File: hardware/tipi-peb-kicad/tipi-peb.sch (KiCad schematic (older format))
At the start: 48 parts, among them Q1 Q_NPN_BCE, T1 TEST_1P, T2 TEST_1P, T3 TEST_1P, T4 TEST_1P, T5 TEST_1P, U1 74HCT138, U2 27C256, U3 74HCT244, U4 74HCT244, U5 74HCT244, U6 XC95144XL-TQ100, U7 74HCT245, U8 LM1117-3.3, U9 LM7805_TO220

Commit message: spread footprints out on peb pcboard.
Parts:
- JTAG1, RPi1: footprint Connect:IDC_Header_Straight_10pins -> Pin_Headers:Pin_Header_Straight_2x05_Pitch2.54mm
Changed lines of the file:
@@
 F 0 "JTAG1" H 14480 1830 50  0000 C CNN
 F 1 "AVR-JTAG-10" H 14310 1170 50  0000 L BNN
-F 2 "Connect:IDC_Header_Straight_10pins" V 14080 1520 50  0001 C CNN
+F 2 "Pin_Headers:Pin_Header_Straight_2x05_Pitch2.54mm" V 14080 1520 50  0001 C CNN
 F 3 "" H 14650 1500 50  0001 C CNN
 	1    14650 1500
@@
 F 0 "RPi1" H 14350 3300 50  0000 C CNN
 F 1 "RPI_CONN_02X05" H 14350 2700 50  0000 C CNN
-F 2 "Connect:IDC_Header_Straight_10pins" H 14350 1800 50  0001 C CNN
+F 2 "Pin_Headers:Pin_Header_Straight_2x05_Pitch2.54mm" H 14350 1800 50  0001 C CNN
 F 3 "" H 14350 1800 50  0001 C CNN
 	1    14350 3000

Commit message: a little layout progress
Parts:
- U1: footprint SMD_Packages:SO-16-W -> Housings_SSOP:SSOP-16_5.3x6.2mm_Pitch0.65mm
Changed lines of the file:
@@
 F 0 "U1" H 1950 9800 50  0000 C CNN
 F 1 "74HCT138" H 2000 8751 50  0000 C CNN
-F 2 "SMD_Packages:SO-16-W" H 1850 9300 50  0001 C CNN
+F 2 "Housings_SSOP:SSOP-16_5.3x6.2mm_Pitch0.65mm" H 1850 9300 50  0001 C CNN
 F 3 "" H 1850 9300 50  0001 C CNN
 	1    1850 9300

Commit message: stash these changes.
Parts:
- U1: footprint Housings_SSOP:SSOP-16_5.3x6.2mm_Pitch0.65mm -> Housings_SSOP:SSOP-16_4.4x5.2mm_Pitch0.65mm
- U3, U4, U5, U7: footprint SMD_Packages:SSOP-20 -> Housings_SSOP:SSOP-20_4.4x6.5mm_Pitch0.65mm
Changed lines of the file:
@@
 F 0 "U7" H 10350 9975 50  0000 L BNN
 F 1 "74HCT245" H 10300 8825 50  0000 L TNN
-F 2 "SMD_Packages:SSOP-20" H 10250 9400 50  0001 C CNN
+F 2 "Housings_SSOP:SSOP-20_4.4x6.5mm_Pitch0.65mm" H 10250 9400 50  0001 C CNN
 F 3 "" H 10250 9400 50  0001 C CNN
 	1    10250 9400
@@
 F 0 "U5" H 8250 10050 50  0000 L CNN
 F 1 "74HCT244" H 8200 8750 50  0000 L CNN
-F 2 "SMD_Packages:SSOP-20" H 8150 9400 50  0001 C CNN
+F 2 "Housings_SSOP:SSOP-20_4.4x6.5mm_Pitch0.65mm" H 8150 9400 50  0001 C CNN
 F 3 "" H 8150 9400 50  0000 C CNN
 	1    8150 9400
@@
 F 0 "U4" H 5900 10050 50  0000 L CNN
 F 1 "74HCT244" H 5850 8750 50  0000 L CNN
-F 2 "SMD_Packages:SSOP-20" H 5800 9400 50  0001 C CNN
+F 2 "Housings_SSOP:SSOP-20_4.4x6.5mm_Pitch0.65mm" H 5800 9400 50  0001 C CNN
 F 3 "" H 5800 9400 50  0000 C CNN
 	1    5800 9400
@@
 F 0 "U3" H 3850 10050 50  0000 L CNN
 F 1 "74HCT244" H 3800 8750 50  0000 L CNN
-F 2 "SMD_Packages:SSOP-20" H 3750 9400 50  0001 C CNN
+F 2 "Housings_SSOP:SSOP-20_4.4x6.5mm_Pitch0.65mm" H 3750 9400 50  0001 C CNN
 F 3 "" H 3750 9400 50  0000 C CNN
 	1    3750 9400
@@
 F 0 "U1" H 1950 9800 50  0000 C CNN
 F 1 "74HCT138" H 2000 8751 50  0000 C CNN
-F 2 "Housings_SSOP:SSOP-16_5.3x6.2mm_Pitch0.65mm" H 1850 9300 50  0001 C CNN
+F 2 "Housings_SSOP:SSOP-16_4.4x5.2mm_Pitch0.65mm" H 1850 9300 50  0001 C CNN
 F 3 "" H 1850 9300 50  0001 C CNN
 	1    1850 9300

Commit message: about half routed
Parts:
- removed T1, T2, T3, T4, T5: TEST_1P, Wire_Pads:SolderWirePad_single_0-8mmDrill, symbol TEST_1P
- U1: footprint Housings_SSOP:SSOP-16_4.4x5.2mm_Pitch0.65mm -> Housings_SSOP:TSSOP-16_4.4x5mm_Pitch0.65mm
- U3, U4, U5, U7: footprint Housings_SSOP:SSOP-20_4.4x6.5mm_Pitch0.65mm -> Housings_SSOP:TSSOP-20_4.4x6.5mm_Pitch0.65mm
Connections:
- no-connect marks 61 -> 66
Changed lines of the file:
@@
 F 0 "U7" H 10350 9975 50  0000 L BNN
 F 1 "74HCT245" H 10300 8825 50  0000 L TNN
-F 2 "Housings_SSOP:SSOP-20_4.4x6.5mm_Pitch0.65mm" H 10250 9400 50  0001 C CNN
+F 2 "Housings_SSOP:TSSOP-20_4.4x6.5mm_Pitch0.65mm" H 10250 9400 50  0001 C CNN
 F 3 "" H 10250 9400 50  0001 C CNN
 	1    10250 9400
@@
 $EndComp
 $Comp
-L TEST_1P T5
-U 1 1 597515DC
-P 14650 2800
-F 0 "T5" H 14650 3070 50  0000 C CNN
-F 1 "TEST_1P" H 14650 3000 50  0000 C CNN
-F 2 "Wire_Pads:SolderWirePad_single_0-8mmDrill" H 14850 2800 50  0001 C CNN
-F 3 "" H 14850 2800 50  0001 C CNN
-	1    14650 2800
-	1    0    0    -1
-$EndComp
-$Comp
-L TEST_1P T4
-U 1 1 5975362C
-P 10200 5600
-F 0 "T4" H 10200 5870 50  0000 C CNN
-F 1 "TEST_1P" H 10200 5800 50  0000 C CNN
-F 2 "Wire_Pads:SolderWirePad_single_0-8mmDrill" H 10400 5600 50  0001 C CNN
-F 3 "" H 10400 5600 50  0001 C CNN
-	1    10200 5600
-	0    1    1    0
-$EndComp
-$Comp
-L TEST_1P T3
-U 1 1 5975393E
-P 10200 5500
-F 0 "T3" H 10200 5770 50  0000 C CNN
-F 1 "TEST_1P" H 10200 5700 50  0000 C CNN
-F 2 "Wire_Pads:SolderWirePad_single_0-8mmDrill" H 10400 5500 50  0001 C CNN
-F 3 "" H 10400 5500 50  0001 C CNN
-	1    10200 5500
-	0    1    1    0
-$EndComp
-$Comp
-L TEST_1P T2
-U 1 1 597539A7
-P 10200 5400
-F 0 "T2" H 10200 5670 50  0000 C CNN
-F 1 "TEST_1P" H 10200 5600 50  0000 C CNN
-F 2 "Wire_Pads:SolderWirePad_single_0-8mmDrill" H 10400 5400 50  0001 C CNN
-F 3 "" H 10400 5400 50  0001 C CNN
-	1    10200 5400
-	0    1    1    0
-$EndComp
-$Comp
-L TEST_1P T1
-U 1 1 59753A11
-P 10200 5300
-F 0 "T1" H 10200 5570 50  0000 C CNN
-F 1 "TEST_1P" H 10200 5500 50  0000 C CNN
-F 2 "Wire_Pads:SolderWirePad_single_0-8mmDrill" H 10400 5300 50  0001 C CNN
-F 3 "" H 10400 5300 50  0001 C CNN
-	1    10200 5300
-	0    1    1    0
-$EndComp
-$Comp
 L R R4
 U 1 1 599E6C64
@@
 F 0 "U5" H 8250 10050 50  0000 L CNN
 F 1 "74HCT244" H 8200 8750 50  0000 L CNN
-F 2 "Housings_SSOP:SSOP-20_4.4x6.5mm_Pitch0.65mm" H 8150 9400 50  0001 C CNN
+F 2 "Housings_SSOP:TSSOP-20_4.4x6.5mm_Pitch0.65mm" H 8150 9400 50  0001 C CNN
 F 3 "" H 8150 9400 50  0000 C CNN
 	1    8150 9400
@@
 F 0 "U4" H 5900 10050 50  0000 L CNN
 F 1 "74HCT244" H 5850 8750 50  0000 L CNN
-F 2 "Housings_SSOP:SSOP-20_4.4x6.5mm_Pitch0.65mm" H 5800 9400 50  0001 C CNN
+F 2 "Housings_SSOP:TSSOP-20_4.4x6.5mm_Pitch0.65mm" H 5800 9400 50  0001 C CNN
 F 3 "" H 5800 9400 50  0000 C CNN
 	1    5800 9400
@@
 F 0 "U3" H 3850 10050 50  0000 L CNN
 F 1 "74HCT244" H 3800 8750 50  0000 L CNN
-F 2 "Housings_SSOP:SSOP-20_4.4x6.5mm_Pitch0.65mm" H 3750 9400 50  0001 C CNN
+F 2 "Housings_SSOP:TSSOP-20_4.4x6.5mm_Pitch0.65mm" H 3750 9400 50  0001 C CNN
 F 3 "" H 3750 9400 50  0000 C CNN
 	1    3750 9400
@@
 Connection ~ 8850 7000
 Wire Wire Line
-	9750 5600 10200 5600
-Wire Wire Line
-	9750 5500 10200 5500
-Wire Wire Line
-	9750 5400 10200 5400
-Wire Wire Line
-	9750 5300 10200 5300
-Wire Wire Line
 	11600 2150 11450 2150
 Wire Wire Line
@@
 F 0 "U1" H 1950 9800 50  0000 C CNN
 F 1 "74HCT138" H 2000 8751 50  0000 C CNN
-F 2 "Housings_SSOP:SSOP-16_4.4x5.2mm_Pitch0.65mm" H 1850 9300 50  0001 C CNN
+F 2 "Housings_SSOP:TSSOP-16_4.4x5mm_Pitch0.65mm" H 1850 9300 50  0001 C CNN
 F 3 "" H 1850 9300 50  0001 C CNN
 	1    1850 9300
@@
 	-1   0    0    1
 $EndComp
+NoConn ~ 9750 5300
+NoConn ~ 9750 5400
+NoConn ~ 9750 5500
+NoConn ~ 9750 5600
+NoConn ~ 14650 2800
 $EndSCHEMATC

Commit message: 2/3rds routed
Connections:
- net +5V: no longer R10.2
- net GND: no longer R11.2
- net TI_AMD: no longer E1.56 (MEMEN*), U1.4 (E1)
- new net TI_MEMEN: E1.56 (MEMEN*), U1.4 (E1)
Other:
- moved on the sheet: R10, R11
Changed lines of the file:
@@
 Text GLabel 2300 6700 2    60   Output ~ 0
 TI_PH3
-Text GLabel 1250 9650 0    60   Input ~ 0
+Text GLabel 1000 9650 0    60   Input ~ 0
 TI_MEMEN
 Text GLabel 4250 8900 2    60   Output ~ 0
@@
 Text GLabel 1200 4700 0    60   Output ~ 0
 TI_AME
-Text GLabel 1050 9550 0    60   Input ~ 0
+Text GLabel 900  9550 0    60   Input ~ 0
 TI_AMD
-Text GLabel 1050 9450 0    60   Input ~ 0
+Text GLabel 900  9450 0    60   Input ~ 0
 TI_AME
 Wire Wire Line
@@
 L R R10
 U 1 1 59EF200E
-P 1100 9950
-F 0 "R10" V 1180 9950 50  0000 C CNN
-F 1 "4.7k" V 1100 9950 50  0000 C CNN
-F 2 "Resistors_SMD:R_0805_HandSoldering" V 1030 9950 50  0001 C CNN
-F 3 "" H 1100 9950 50  0001 C CNN
-	1    1100 9950
+P 1050 9950
+F 0 "R10" V 1130 9950 50  0000 C CNN
+F 1 "4.7k" V 1050 9950 50  0000 C CNN
+F 2 "Resistors_SMD:R_0805_HandSoldering" V 980 9950 50  0001 C CNN
+F 3 "" H 1050 9950 50  0001 C CNN
+	1    1050 9950
 	1    0    0    -1
 $EndComp
@@
 L R R11
 U 1 1 59EF20E5
-P 1250 9950
-F 0 "R11" V 1330 9950 50  0000 C CNN
-F 1 "4.7k" V 1250 9950 50  0000 C CNN
-F 2 "Resistors_SMD:R_0805_HandSoldering" V 1180 9950 50  0001 C CNN
-F 3 "" H 1250 9950 50  0001 C CNN
-	1    1250 9950
+P 1200 9950
+F 0 "R11" V 1280 9950 50  0000 C CNN
+F 1 "4.7k" V 1200 9950 50  0000 C CNN
+F 2 "Resistors_SMD:R_0805_HandSoldering" V 1130 9950 50  0001 C CNN
+F 3 "" H 1200 9950 50  0001 C CNN
+	1    1200 9950
 	1    0    0    -1
 $EndComp
@@
 L GND #PWR050
 U 1 1 59EF22F3
-P 1250 10100
-F 0 "#PWR050" H 1250 9850 50  0001 C CNN
-F 1 "GND" H 1250 9950 50  0000 C CNN
-F 2 "" H 1250 10100 50  0001 C CNN
-F 3 "" H 1250 10100 50  0001 C CNN
-	1    1250 10100
+P 1200 10150
+F 0 "#PWR050" H 1200 9900 50  0001 C CNN
+F 1 "GND" H 1200 10000 50  0000 C CNN
+F 2 "" H 1200 10150 50  0001 C CNN
+F 3 "" H 1200 10150 50  0001 C CNN
+	1    1200 10150
 	1    0    0    -1
 $EndComp
@@
 L +5V #PWR051
 U 1 1 59EF241E
-P 1100 10100
-F 0 "#PWR051" H 1100 9950 50  0001 C CNN
-F 1 "+5V" H 1100 10240 50  0000 C CNN
-F 2 "" H 1100 10100 50  0001 C CNN
-F 3 "" H 1100 10100 50  0001 C CNN
-	1    1100 10100
+P 1050 10150
+F 0 "#PWR051" H 1050 10000 50  0001 C CNN
+F 1 "+5V" H 1050 10290 50  0000 C CNN
+F 2 "" H 1050 10150 50  0001 C CNN
+F 3 "" H 1050 10150 50  0001 C CNN
+	1    1050 10150
 	-1   0    0    1
 $EndComp
-Wire Wire Line
-	1250 9800 1250 9550
-Wire Wire Line
-	1250 9550 1050 9550
-Wire Wire Line
-	1100 9800 1100 9450
-Wire Wire Line
-	1050 9450 1250 9450
-Connection ~ 1100 9450
-Connection ~ 1250 9550
 $Comp
 L GND #PWR052
@@
 NoConn ~ 9750 5600
 NoConn ~ 14650 2800
+Wire Wire Line
+	1000 9650 1250 9650
+Wire Wire Line
+	1200 9800 1200 9550
+Wire Wire Line
+	900  9550 1250 9550
+Connection ~ 1200 9550
+Wire Wire Line
+	1250 9450 900  9450
+Wire Wire Line
+	1050 9800 1050 9450
+Connection ~ 1050 9450
 $EndSCHEMATC

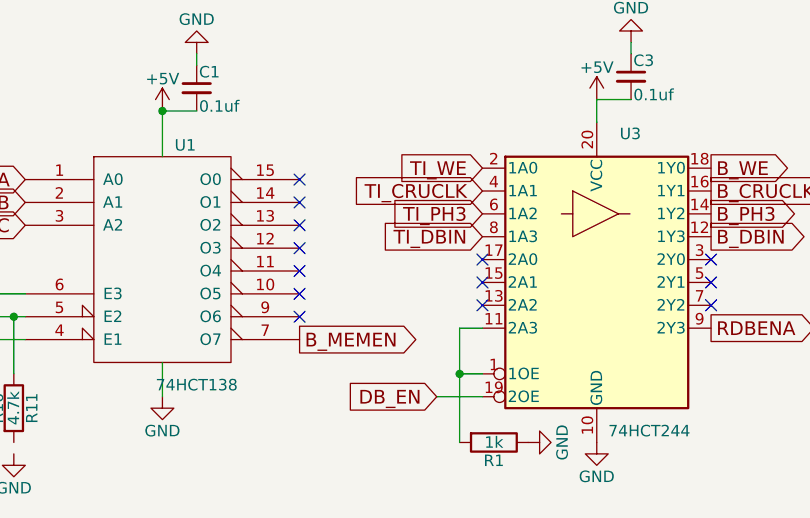
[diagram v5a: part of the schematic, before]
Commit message: just power lines left
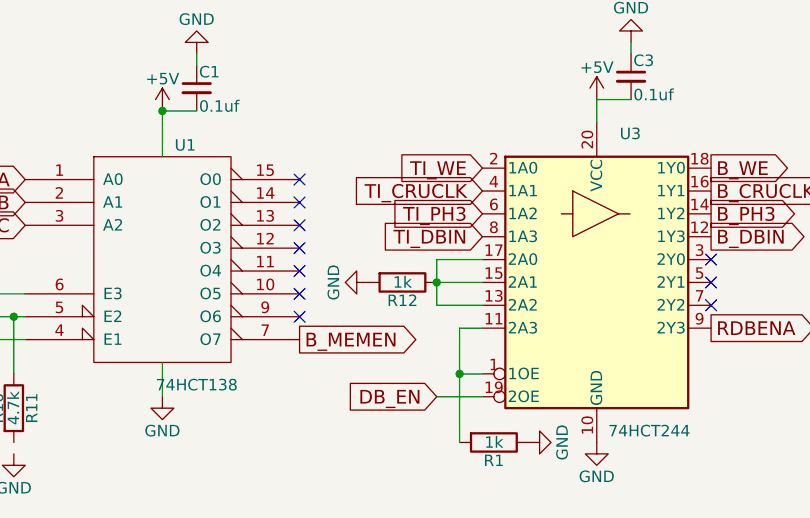
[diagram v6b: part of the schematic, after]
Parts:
- added R12: 1k, Resistors_SMD:R_0805_HandSoldering, symbol R
- U8, U9: footprint TO_SOT_Packages_SMD:SOT-223 -> TO_SOT_Packages_SMD:SOT-223-3_TabPin2
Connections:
- net GND: now also R12.2
- net at U3.13 (2A2): now also U3.15 (2A1), U3.17 (2A0), R12.1
- no-connect marks 66 -> 63
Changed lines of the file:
@@
 F 0 "U8" H 14550 4000 50  0000 C CNN
 F 1 "LM1117-3.3" H 14450 4500 50  0000 C CNN
-F 2 "TO_SOT_Packages_SMD:SOT-223" H 14450 4250 50  0001 C CNN
+F 2 "TO_SOT_Packages_SMD:SOT-223-3_TabPin2" H 14450 4250 50  0001 C CNN
 F 3 "" H 14450 4250 50  0001 C CNN
 	1    14450 4250
@@
 F 0 "U9" H 14300 5325 50  0000 C CNN
 F 1 "LM7805_TO220" H 14450 5325 50  0000 L CNN
-F 2 "TO_SOT_Packages_SMD:SOT-223" H 14450 5425 50  0001 C CIN
+F 2 "TO_SOT_Packages_SMD:SOT-223-3_TabPin2" H 14450 5425 50  0001 C CIN
 F 3 "" H 14450 5150 50  0001 C CNN
 	1    14450 5200
@@
 	0    1    1    0
 $EndComp
-NoConn ~ 3250 9300
-NoConn ~ 3250 9400
-NoConn ~ 3250 9500
 NoConn ~ 4250 9300
 NoConn ~ 4250 9400
@@
 	1050 9800 1050 9450
 Connection ~ 1050 9450
+$Comp
+L R R12
+U 1 1 5ADB77AD
+P 2900 9400
+F 0 "R12" V 2980 9400 50  0000 C CNN
+F 1 "1k" V 2900 9400 50  0000 C CNN
+F 2 "Resistors_SMD:R_0805_HandSoldering" V 2830 9400 50  0001 C CNN
+F 3 "" H 2900 9400 50  0001 C CNN
+	1    2900 9400
+	0    1    1    0
+$EndComp
+$Comp
+L GND #PWR053
+U 1 1 5ADB786B
+P 2750 9400
+F 0 "#PWR053" H 2750 9150 50  0001 C CNN
+F 1 "GND" H 2750 9250 50  0000 C CNN
+F 2 "" H 2750 9400 50  0001 C CNN
+F 3 "" H 2750 9400 50  0001 C CNN
+	1    2750 9400
+	0    1    1    0
+$EndComp
+Wire Wire Line
+	3250 9300 3050 9300
+Wire Wire Line
+	3050 9300 3050 9500
+Wire Wire Line
+	3050 9500 3250 9500
+Connection ~ 3050 9400
+Wire Wire Line
+	3250 9400 3050 9400
 $EndSCHEMATC

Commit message: adjust page layout
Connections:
- net +5V: now also R10.2
- net GND: now also R11.2
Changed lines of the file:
@@
 L GND #PWR022
 U 1 1 596F5164
-P 9000 7000
-F 0 "#PWR022" H 9000 6750 50  0001 C CNN
-F 1 "GND" H 9000 6850 50  0000 C CNN
-F 2 "" H 9000 7000 50  0001 C CNN
-F 3 "" H 9000 7000 50  0001 C CNN
-	1    9000 7000
+P 9000 7050
+F 0 "#PWR022" H 9000 6800 50  0001 C CNN
+F 1 "GND" H 9000 6900 50  0000 C CNN
+F 2 "" H 9000 7050 50  0001 C CNN
+F 3 "" H 9000 7050 50  0001 C CNN
+	1    9000 7050
 	1    0    0    -1
 $EndComp
@@
 	14000 3200 14150 3200
 Wire Wire Line
-	14650 2900 15100 2900
-Wire Wire Line
 	2050 1100 2050 1150
 Wire Wire Line
@@
 Connection ~ 9000 950
 Connection ~ 9250 950
-Wire Wire Line
-	8150 7000 9000 7000
-Connection ~ 8250 7000
-Connection ~ 8350 7000
-Connection ~ 8450 7000
-Connection ~ 8550 7000
-Connection ~ 8650 7000
-Connection ~ 8750 7000
-Connection ~ 8850 7000
 Wire Wire Line
 	11600 2150 11450 2150
@@
 Wire Wire Line
 	1850 8650 1850 8850
-Wire Wire Line
-	2000 8450 2000 8400
 Connection ~ 1850 8650
 $Comp
@@
 $Comp
 L GND #PWR033
-U 1 1 59C76FD1
-P 5800 10100
-F 0 "#PWR033" H 5800 9850 50  0001 C CNN
-F 1 "GND" H 5800 9950 50  0000 C CNN
-F 2 "" H 5800 10100 50  0001 C CNN
-F 3 "" H 5800 10100 50  0001 C CNN
-	1    5800 10100
-	1    0    0    -1
-$EndComp
-$Comp
-L GND #PWR034
 U 1 1 59C7705D
 P 3750 10100
-F 0 "#PWR034" H 3750 9850 50  0001 C CNN
+F 0 "#PWR033" H 3750 9850 50  0001 C CNN
 F 1 "GND" H 3750 9950 50  0000 C CNN
 F 2 "" H 3750 10100 50  0001 C CNN
@@
 	2300 5200 2600 5200
 $Comp
-L +8V #PWR035
+L +8V #PWR034
 U 1 1 59E1955F
 P 1200 4300
-F 0 "#PWR035" H 1200 4150 50  0001 C CNN
+F 0 "#PWR034" H 1200 4150 50  0001 C CNN
 F 1 "+8V" H 1200 4440 50  0000 C CNN
 F 2 "" H 1200 4300 50  0001 C CNN
@@
 $EndComp
 $Comp
-L +8V #PWR036
+L +8V #PWR035
 U 1 1 59E1A127
 P 13900 4250
-F 0 "#PWR036" H 13900 4100 50  0001 C CNN
+F 0 "#PWR035" H 13900 4100 50  0001 C CNN
 F 1 "+8V" H 13900 4390 50  0000 C CNN
 F 2 "" H 13900 4250 50  0001 C CNN
@@
 $EndComp
 $Comp
-L +8V #PWR037
+L +8V #PWR036
 U 1 1 59E1BE02
 P 13950 5200
-F 0 "#PWR037" H 13950 5050 50  0001 C CNN
+F 0 "#PWR036" H 13950 5050 50  0001 C CNN
 F 1 "+8V" H 13950 5340 50  0000 C CNN
 F 2 "" H 13950 5200 50  0001 C CNN
@@
 $EndComp
 $Comp
-L GND #PWR038
+L GND #PWR037
 U 1 1 59E1BFF6
-P 14450 5600
-F 0 "#PWR038" H 14450 5350 50  0001 C CNN
-F 1 "GND" H 14450 5450 50  0000 C CNN
-F 2 "" H 14450 5600 50  0001 C CNN
-F 3 "" H 14450 5600 50  0001 C CNN
-	1    14450 5600
-	1    0    0    -1
-$EndComp
-$Comp
-L +5V #PWR039
+P 14450 5650
+F 0 "#PWR037" H 14450 5400 50  0001 C CNN
+F 1 "GND" H 14450 5500 50  0000 C CNN
+F 2 "" H 14450 5650 50  0001 C CNN
+F 3 "" H 14450 5650 50  0001 C CNN
+	1    14450 5650
+	1    0    0    -1
+$EndComp
+$Comp
+L +5V #PWR038
 U 1 1 59E1C3C9
 P 15000 5200
-F 0 "#PWR039" H 15000 5050 50  0001 C CNN
+F 0 "#PWR038" H 15000 5050 50  0001 C CNN
 F 1 "+5V" H 15000 5340 50  0000 C CNN
 F 2 "" H 15000 5200 50  0001 C CNN
@@
 Wire Wire Line
 	14850 5550 14850 5400
-Wire Wire Line
-	14450 5500 14450 5600
 Connection ~ 14450 5550
 Text GLabel 7350 2900 0    60   Input ~ 0
@@
 NoConn ~ 2300 7200
 $Comp
-L GND #PWR040
+L GND #PWR039
 U 1 1 59E4A124
 P 2600 5200
-F 0 "#PWR040" H 2600 4950 50  0001 C CNN
+F 0 "#PWR039" H 2600 4950 50  0001 C CNN
 F 1 "GND" H 2600 5050 50  0000 C CNN
 F 2 "" H 2600 5200 50  0001 C CNN
@@
 $EndComp
 $Comp
-L GND #PWR041
+L GND #PWR040
 U 1 1 59E4AF1D
 P 1200 4400
-F 0 "#PWR041" H 1200 4150 50  0001 C CNN
+F 0 "#PWR040" H 1200 4150 50  0001 C CNN
 F 1 "GND" H 1200 4250 50  0000 C CNN
 F 2 "" H 1200 4400 50  0001 C CNN
@@
 $EndComp
 $Comp
-L GND #PWR042
+L GND #PWR041
 U 1 1 59E4B3D4
 P 1200 4500
-F 0 "#PWR042" H 1200 4250 50  0001 C CNN
+F 0 "#PWR041" H 1200 4250 50  0001 C CNN
 F 1 "GND" H 1200 4350 50  0000 C CNN
 F 2 "" H 1200 4500 50  0001 C CNN
@@
 $EndComp
 $Comp
-L GND #PWR043
+L GND #PWR042
 U 1 1 59E4B469
 P 1200 4600
-F 0 "#PWR043" H 1200 4350 50  0001 C CNN
+F 0 "#PWR042" H 1200 4350 50  0001 C CNN
 F 1 "GND" H 1200 4450 50  0000 C CNN
 F 2 "" H 1200 4600 50  0001 C CNN
@@
 $EndComp
 $Comp
-L GND #PWR044
+L GND #PWR043
 U 1 1 59E4B4FE
 P 850 5600
-F 0 "#PWR044" H 850 5350 50  0001 C CNN
+F 0 "#PWR043" H 850 5350 50  0001 C CNN
 F 1 "GND" H 850 5450 50  0000 C CNN
 F 2 "" H 850 5600 50  0001 C CNN
@@
 $EndComp
 $Comp
-L GND #PWR045
+L GND #PWR044
 U 1 1 59E4B9B5
 P 850 6600
-F 0 "#PWR045" H 850 6350 50  0001 C CNN
+F 0 "#PWR044" H 850 6350 50  0001 C CNN
 F 1 "GND" H 850 6450 50  0000 C CNN
 F 2 "" H 850 6600 50  0001 C CNN
@@
 $EndComp
 $Comp
-L GND #PWR046
+L GND #PWR045
 U 1 1 59E4BB30
 P 1000 6700
-F 0 "#PWR046" H 1000 6450 50  0001 C CNN
+F 0 "#PWR045" H 1000 6450 50  0001 C CNN
 F 1 "GND" H 1000 6550 50  0000 C CNN
 F 2 "" H 1000 6700 50  0001 C CNN
@@
 $EndComp
 $Comp
-L GND #PWR047
+L GND #PWR046
 U 1 1 59E4BBC5
 P 950 6900
-F 0 "#PWR047" H 950 6650 50  0001 C CNN
+F 0 "#PWR046" H 950 6650 50  0001 C CNN
 F 1 "GND" H 950 6750 50  0000 C CNN
 F 2 "" H 950 6900 50  0001 C CNN
@@
 NoConn ~ 2450 8950
 $Comp
-L GND #PWR048
+L GND #PWR047
 U 1 1 59E3C0E9
 P 1850 9900
-F 0 "#PWR048" H 1850 9650 50  0001 C CNN
+F 0 "#PWR047" H 1850 9650 50  0001 C CNN
 F 1 "GND" H 1850 9750 50  0000 C CNN
 F 2 "" H 1850 9900 50  0001 C CNN
@@
 	1850 9900 1850 9750
 $Comp
-L GND #PWR049
+L GND #PWR048
 U 1 1 59E3C39E
 P 8150 10100
-F 0 "#PWR049" H 8150 9850 50  0001 C CNN
+F 0 "#PWR048" H 8150 9850 50  0001 C CNN
 F 1 "GND" H 8150 9950 50  0000 C CNN
 F 2 "" H 8150 10100 50  0001 C CNN
@@
 $EndComp
 $Comp
-L GND #PWR050
+L GND #PWR049
 U 1 1 59EF22F3
 P 1200 10150
-F 0 "#PWR050" H 1200 9900 50  0001 C CNN
+F 0 "#PWR049" H 1200 9900 50  0001 C CNN
 F 1 "GND" H 1200 10000 50  0000 C CNN
 F 2 "" H 1200 10150 50  0001 C CNN
@@
 $EndComp
 $Comp
-L +5V #PWR051
+L +5V #PWR050
 U 1 1 59EF241E
 P 1050 10150
-F 0 "#PWR051" H 1050 10000 50  0001 C CNN
+F 0 "#PWR050" H 1050 10000 50  0001 C CNN
 F 1 "+5V" H 1050 10290 50  0000 C CNN
 F 2 "" H 1050 10150 50  0001 C CNN
@@
 $EndComp
 $Comp
-L GND #PWR052
+L GND #PWR051
 U 1 1 59EF80F6
 P 2000 8400
-F 0 "#PWR052" H 2000 8150 50  0001 C CNN
+F 0 "#PWR051" H 2000 8150 50  0001 C CNN
 F 1 "GND" H 2000 8250 50  0000 C CNN
 F 2 "" H 2000 8400 50  0001 C CNN
@@
 $EndComp
 $Comp
-L GND #PWR053
+L GND #PWR052
 U 1 1 5ADB786B
 P 2750 9400
-F 0 "#PWR053" H 2750 9150 50  0001 C CNN
+F 0 "#PWR052" H 2750 9150 50  0001 C CNN
 F 1 "GND" H 2750 9250 50  0000 C CNN
 F 2 "" H 2750 9400 50  0001 C CNN
@@
 Wire Wire Line
 	3250 9400 3050 9400
+Wire Wire Line
+	1200 10100 1200 10150
+Wire Wire Line
+	1050 10100 1050 10150
+Wire Wire Line
+	14450 5500 14450 5650
+Wire Wire Line
+	5800 10100 5650 10100
+Wire Wire Line
+	5650 10100 5650 10150
+Wire Wire Line
+	5650 10150 5500 10150
+Wire Wire Line
+	5500 10150 5500 10050
+Wire Wire Line
+	2000 8400 2000 8450
+Wire Wire Line
+	9000 7050 8150 7050
+Wire Wire Line
+	8150 7050 8150 7000
+Wire Wire Line
+	8250 7000 8250 7050
+Connection ~ 8250 7050
+Wire Wire Line
+	8350 7000 8350 7050
+Connection ~ 8350 7050
+Wire Wire Line
+	8450 7000 8450 7050
+Connection ~ 8450 7050
+Wire Wire Line
+	8550 7000 8550 7050
+Connection ~ 8550 7050
+Wire Wire Line
+	8650 7000 8650 7050
+Connection ~ 8650 7050
+Wire Wire Line
+	8750 7000 8750 7050
+Connection ~ 8750 7050
+Wire Wire Line
+	8850 7000 8850 7050
+Connection ~ 8850 7050
+Wire Wire Line
+	14650 2900 15100 2900
 $EndSCHEMATC

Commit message: Fix to work on 4A.
Jumper added to disconnect SCLK/AMD line on 4As.
Pull-up resister added to boost power on r_din transmission line.
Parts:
- added JP1: Jumper_NO_Small, Pin_Headers:Pin_Header_Straight_2x01_Pitch2.54mm, symbol Jumper_NO_Small
- added R13: 10k, Resistors_SMD:R_0805_HandSoldering, symbol R
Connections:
- net +3V3: now also R13.2
- net R_DIN: now also R13.1
- net TI_AMD: now also JP1.2; no longer R11.1, U1.5 (E2)
- new net: JP1.1, R11.1, U1.5 (E2)
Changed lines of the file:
@@
 Text GLabel 14650 3000 2    60   Output ~ 0
 R_DOUT
-Text GLabel 14650 3100 2    60   Input ~ 0
+Text GLabel 15050 3100 2    60   Input ~ 0
 R_DIN
 Text GLabel 14150 2900 0    60   Output ~ 0
@@
 Text Notes 15100 3050 0    60   ~ 0
 GPIO_16
-Text Notes 15100 3150 0    60   ~ 0
+Text Notes 15400 3150 0    60   ~ 0
 GPIO_20
 Text Notes 15100 3250 0    60   ~ 0
@@
 Text GLabel 1200 4700 0    60   Output ~ 0
 TI_AME
-Text GLabel 900  9550 0    60   Input ~ 0
+Text GLabel 600  10050 3    60   Input ~ 0
 TI_AMD
 Text GLabel 900  9450 0    60   Input ~ 0
@@
 	1200 9800 1200 9550
 Wire Wire Line
-	900  9550 1250 9550
+	600  9550 1250 9550
 Connection ~ 1200 9550
 Wire Wire Line
@@
 Wire Wire Line
 	14650 2900 15100 2900
+$Comp
+L +3.3V #PWR053
+U 1 1 5B0C349D
+P 15150 3650
+F 0 "#PWR053" H 15150 3500 50  0001 C CNN
+F 1 "+3.3V" H 15150 3790 50  0000 C CNN
+F 2 "" H 15150 3650 50  0001 C CNN
+F 3 "" H 15150 3650 50  0001 C CNN
+	1    15150 3650
+	0    1    1    0
+$EndComp
+Wire Wire Line
+	15050 3100 14650 3100
+Wire Wire Line
+	15000 3350 15000 3100
+Connection ~ 15000 3100
+$Comp
+L R R13
+U 1 1 5B0C3DBA
+P 15000 3500
+F 0 "R13" V 15080 3500 50  0000 C CNN
+F 1 "10k" V 15000 3500 50  0000 C CNN
+F 2 "Resistors_SMD:R_0805_HandSoldering" V 14930 3500 50  0001 C CNN
+F 3 "" H 15000 3500 50  0001 C CNN
+	1    15000 3500
+	1    0    0    -1
+$EndComp
+Wire Wire Line
+	15000 3650 15150 3650
+$Comp
+L Jumper_NO_Small JP1
+U 1 1 5B106100
+P 600 9900
+F 0 "JP1" H 600 9980 50  0000 C CNN
+F 1 "Jumper_NO_Small" H 610 9840 50  0000 C CNN
+F 2 "Pin_Headers:Pin_Header_Straight_2x01_Pitch2.54mm" H 600 9900 50  0001 C CNN
+F 3 "" H 600 9900 50  0001 C CNN
+	1    600  9900
+	0    1    1    0
+$EndComp
+Wire Wire Line
+	600  10050 600  10000
+Wire Wire Line
+	600  9800 600  9550
 $EndSCHEMATC
